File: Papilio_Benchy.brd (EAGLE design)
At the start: 101.6 x 90.2 mm, 123 parts, among them IC1 FT2232H, IC2 93C46, J1 USB MICRO, SW1 EVQQ2, U1 ATMEGA32U4-XUMU, U2 LTC3419EMS, U3 ATMEGA32U4-XUAU, U5 ARDUINO_MEGA_SHIELD, X2 12MHz, Y1 16MHz KX-7

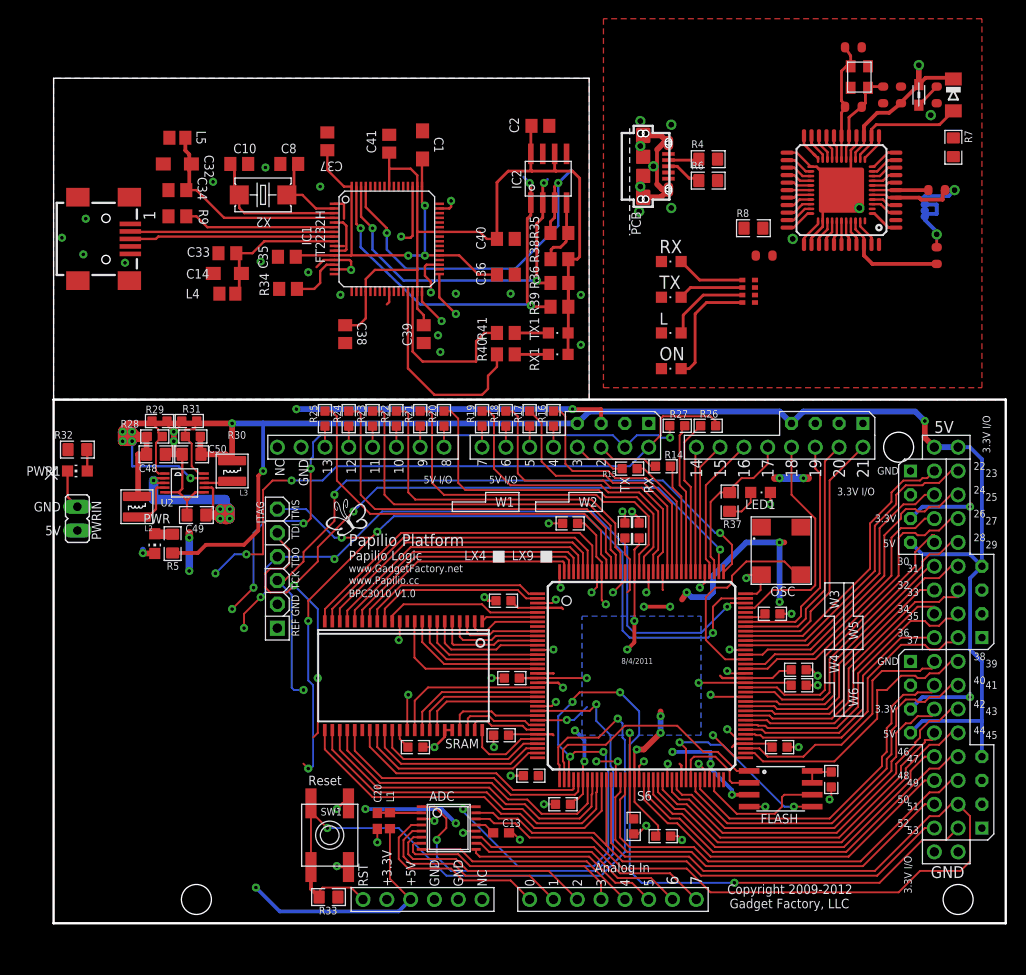
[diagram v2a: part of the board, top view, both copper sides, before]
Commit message: Connections added and blocks placed.
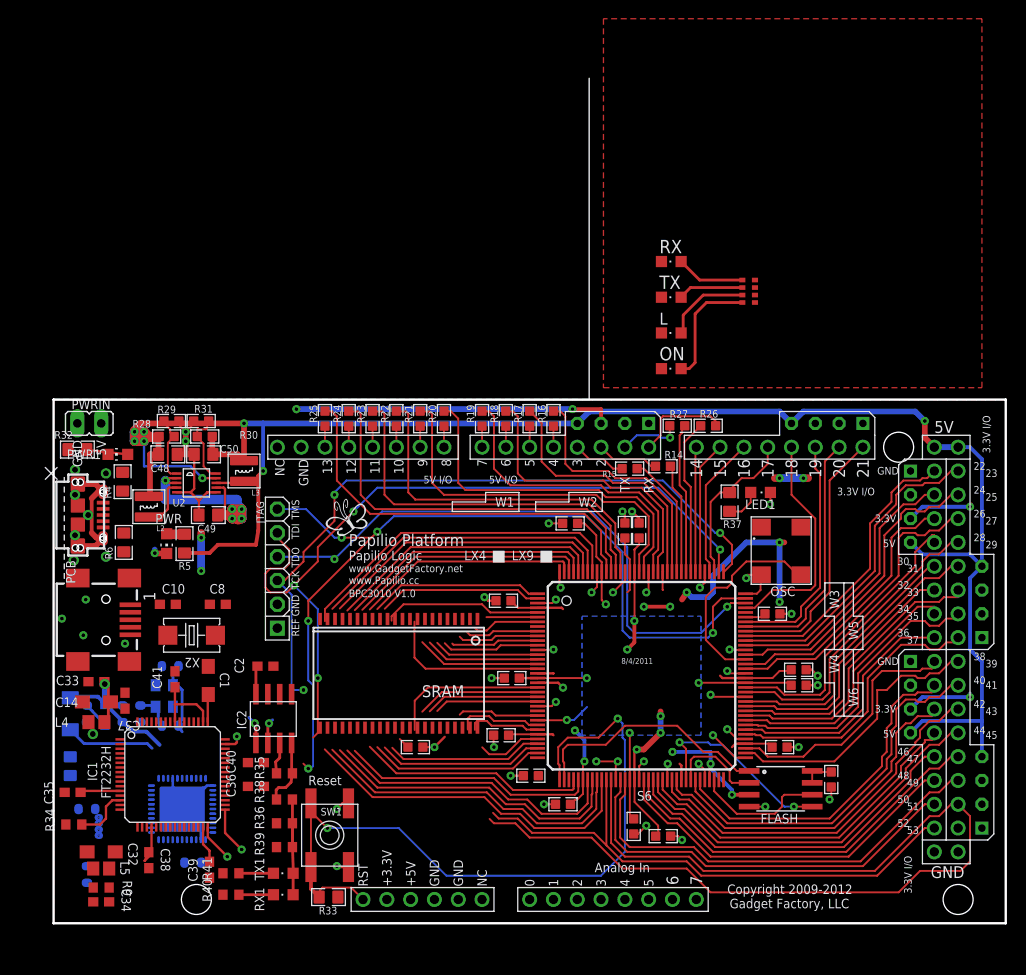
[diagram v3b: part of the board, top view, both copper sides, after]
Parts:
- removed ADC: ADC088S102CIMT, spiadc:TSSOP16
- removed C13, C20: .1uF, rcl:C0603
- removed L1: FERRITEBEAD, rcl:R0603
- removed R8: 10K, GadgetFactory_6.0:0805
- removed U3: ATMEGA32U4-XUAU, SmartPrj:TQFP44-PAD
- C10, C2, C33, C34, C35, C36, C37, C38, C39, C40, C41, C8: device dp_devices:C805 -> dp_devices:C603
- L4, L5: device dp_devices:FB805 -> dp_devices:FB603
- R34, R35, R36, R38, R39, R40, R41, R9: device dp_devices:R805 -> dp_devices:R603
- SRAM: value IS61WV25616 -> ISSI_SRAM_8BIT; device Bogdan_Commons:TSOP44-II -> GadgetFactory:TSOP44-II
- moved D2 115.1 mm to (1.78, 21.1), flipped to the bottom
- moved R7 115.1 mm to (1.78, 15.5), flipped to the bottom
- moved C5 112.2 mm to (3.56, 21.1), flipped to the bottom
- moved C6 112.2 mm to (3.56, 3.94), flipped to the bottom
- moved C7 112.2 mm to (3.56, 10.9), flipped to the bottom
- moved R2 110.1 mm to (4.83, 8.74)
- moved R3 110.1 mm to (4.83, 9.37)
- moved L6 109.1 mm to (5.46, 21.1), flipped to the bottom
- moved C3 106.1 mm to (7.37, 21.1), flipped to the bottom
- moved C9 103.2 mm to (9.27, 21.1), flipped to the bottom
- moved Y1 99.3 mm to (11.8, 23.0), flipped to the bottom
- moved C11 98.4 mm to (12.4, 26.2), flipped to the bottom
- moved R1 98.4 mm to (12.4, 19.8), flipped to the bottom
- moved U1 96.5 mm to (13.7, 10.9), flipped to the bottom
- moved C4 88.9 mm to (14.9, 5.21), flipped to the bottom
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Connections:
- removed net AD0: IC1.16
- removed net AD1: IC1.17
- removed net AD2: IC1.18
- removed net AD3: IC1.19
- removed net ADC_CS: ADC.1, S6.26
- removed net BD0: IC1.38
- removed net BD1: IC1.39
- removed net BD2: IC1.40
- removed net BD3: IC1.41
- removed net D0/RX: U1.20, U3.20
- removed net D1/TX: U1.21, U3.21
- removed net D10: S6.34, SRAM.31
- removed net D11: S6.33, SRAM.32
- removed net D12: S6.21, SRAM.35
- removed net D13: S6.22, SRAM.36
- removed net D14: S6.23, SRAM.37
- removed net D15: S6.24, SRAM.38
- removed net D2/SDA: U1.19, U3.19
- removed net D3/SCL: U1.18, U3.18
- removed net D5*: U1.31, U3.31
- removed net D6*: U1.27, U3.27
- removed net D8: S6.40, SRAM.29
- removed net D9: S6.35, SRAM.30
- removed net HWB: R8.2, U1.33, U3.33
- removed net IO10*: U1.30, U3.30
- removed net IO11*: U1.12, U3.12
- removed net IO12: U1.26, U3.26
- removed net IO13*: RN2.2, U1.32, U3.32
- removed net IO8: U1.28, U3.28
- removed net IO9*: U1.29, U3.29
- removed net MISO: U1.11, U3.11
- removed net MOSI: U1.10, U3.10
- removed net N$10: ADC.2, C20.1, L1.1
- removed net NC: S6.8
- removed net RXLED: RX.C, U1.8, U3.8
- removed net SCK: U1.9, U3.9
- removed net TCK: S6.109, U$2.JTAG_TCK
- removed net TDI: S6.110, U$2.JTAG_TDI
- removed net TDO: S6.106, U$2.JTAG_TDO
- removed net TMS: S6.107, U$2.JTAG_TMS
- removed net TXLED: TX.C, U1.22, U3.22
- new net A18: S6.40, SRAM.41
- new net A19: S6.35, SRAM.25
- new net A20: S6.33, SRAM.42
- new net AD0-JTAG_TCK: IC1.16, S6.109, S6.8, U$2.JTAG_TCK
- new net AD1-JTAG_TDI: IC1.17, S6.110, S6.22, U$2.JTAG_TDI
- new net AD2-JTAG_TDO: IC1.18, S6.106, U$2.JTAG_TDO
- new net AD3-JTAG_TMS: IC1.19, S6.107, U$2.JTAG_TMS
- new net ARDUINO_RESET: D2.A, R7.1, S6.34, U1.13
- new net ATMEGA_A0: U1.36
- new net ATMEGA_A1: U1.37
- new net ATMEGA_A2: U1.38
- new net ATMEGA_A3: U1.39
- new net ATMEGA_A4: U1.40
- new net ATMEGA_A5: U1.41
- new net ATMEGA_D0/RX: U1.20
- new net ATMEGA_D1/TX: U1.21
- new net ATMEGA_D2/SDA: U1.19
- new net ATMEGA_D3/SCL: U1.18
- new net ATMEGA_D4: U1.25
- new net ATMEGA_D5*: U1.31
- new net ATMEGA_D6*: U1.27
- new net ATMEGA_D7: U1.1
- new net ATMEGA_HWB: U1.33
- new net ATMEGA_IO10*: U1.30
- new net ATMEGA_IO11*: U1.12
- new net ATMEGA_IO12: U1.26
- new net ATMEGA_IO13*: RN2.2, U1.32
- new net ATMEGA_IO8: U1.28
- new net ATMEGA_IO9*: U1.29
- new net ATMEGA_MISO: U1.11
- new net ATMEGA_MOSI: U1.10
- new net ATMEGA_RXLED: RX.C, U1.8
- new net ATMEGA_SCK: U1.9
- new net ATMEGA_TXLED: TX.C, U1.22
- new net BD0_MPSSE_TCK: IC1.38, S6.21
- new net BD1_MPSSE_TDI: IC1.39, S6.24
- new net BD2_MPSSE_TDO: IC1.40, S6.23
- new net BD3_MPSSE_TMS: IC1.41, S6.26
- net +5V: no longer U3.14, U3.2, U3.34
- net 3V3: no longer ADC.13, C13.1, SRAM.11, SRAM.33
- net 5V0: no longer L1.2
- net A0: now also SRAM.3; no longer SRAM.1, U1.36, U3.36
- net A1: now also SRAM.4; no longer SRAM.2, U1.37, U3.37
- net A10: now also SRAM.26; no longer SRAM.23
- net A11: now also SRAM.27; no longer SRAM.24
- net A12: now also SRAM.28; no longer SRAM.25
- net A13: now also SRAM.29; no longer SRAM.26
- net A14: now also SRAM.30; no longer SRAM.27
- net A15: now also SRAM.38; no longer SRAM.42
- net A16: now also SRAM.39; no longer SRAM.43
- net A17: now also SRAM.40; no longer SRAM.44
- net A2: now also SRAM.5; no longer SRAM.3, U1.38, U3.38
- net A3: now also SRAM.6; no longer SRAM.4, U1.39, U3.39
- net A4: now also SRAM.7; no longer SRAM.5, U1.40, U3.40
- net A5: now also SRAM.16; no longer SRAM.18, U1.41, U3.41
- net A6: now also SRAM.17; no longer SRAM.19
- net A7: now also SRAM.18; no longer SRAM.20
- net A8: now also SRAM.19; no longer SRAM.21
- net A9: now also SRAM.20; no longer SRAM.22
- net AGND: no longer U3.43
- net AREF: no longer U3.42
- net AVCC: no longer U3.24, U3.44
- net CS: now also SRAM.8; no longer SRAM.6
- net D0: now also SRAM.9; no longer SRAM.7
- net D1: now also SRAM.10; no longer SRAM.8
- net D2: now also SRAM.13; no longer SRAM.9
- net D3: now also SRAM.14; no longer SRAM.10
- net D4: now also SRAM.31; no longer SRAM.13, U1.25, U3.25
- net D5: now also SRAM.32; no longer SRAM.14
- net D6: now also SRAM.35; no longer SRAM.15
- net D7: now also SRAM.36; no longer SRAM.16, U1.1, U3.1
- net GND: no longer ADC.12, ADC.3, C13.2, C20.2, R8.1, SRAM.39, SRAM.40, U3.15, U3.23, U3.35, U3.P$1
- net MEGA_A0: no longer ADC.4
- net MEGA_A1: no longer ADC.5
- net MEGA_A2: no longer ADC.6
- net MEGA_A3: no longer ADC.7
- net MEGA_A4: no longer ADC.8
- net MEGA_A5: no longer ADC.9
- net MEGA_A6: no longer ADC.10
- net MEGA_A7: no longer ADC.11
- net MEGA_D51: no longer ADC.14
- net MEGA_D52: no longer ADC.15
- net MEGA_D53: no longer ADC.16
- net OE: now also SRAM.37; no longer SRAM.41
- net RD+: no longer U3.4
- net RD-: no longer U3.3
- net RESET: no longer D2.A, R7.1, U1.13, U3.13
- net UCAP: no longer U3.6
- net UGND: no longer U3.5
- net VUSB: no longer U3.7
- net WE: now also SRAM.15; no longer SRAM.17
- net XTAL1: no longer U3.17
- net XTAL2: no longer U3.16
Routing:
- net MEGA_D53: track 108.4 -> 0.00 mm, vias 6 -> 0
- net AD1-JTAG_TDI: track 0.00 -> 98.7 mm, vias 0 -> 4
- net TMS: track 94.5 -> 0.00 mm, vias 5 -> 0
- net AD3-JTAG_TMS: track 0.00 -> 94.5 mm, vias 0 -> 5
- net TDI: track 85.5 -> 0.00 mm, vias 4 -> 0
- net TCK: track 74.9 -> 0.00 mm, vias 3 -> 0
- net AD0-JTAG_TCK: track 0.00 -> 74.9 mm, vias 0 -> 3
- net TDO: track 73.2 -> 0.00 mm, vias 4 -> 0
- net AD2-JTAG_TDO: track 0.00 -> 64.1 mm, vias 0 -> 2
- net GND: track 188.1 -> 124.5 mm, vias 78 -> 55
- net USB_RXD: track 65.1 -> 6.74 mm, vias 5 -> 1
- net 3.3V: track 89.5 -> 32.9 mm
- net USB_TXD: track 66.1 -> 10.3 mm, vias 3 -> 0
- net ADC_CS: track 51.1 -> 0.00 mm, vias 2 -> 0
- net EECS: track 43.8 -> 3.04 mm, vias 3 -> 1
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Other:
- outline, holes or cut-outs redrawn
- board text removed: "!PWEREN"
- board text removed: "!RESET"
- board text removed: "1.8V"
- board text removed: "3V3"
- board text removed: "ACBUS0"
- board text removed: "ACBUS1"
- board text removed: "ACBUS2"
- board text removed: "ACBUS3"
- board text removed: "ACBUS4"
- board text removed: "ACBUS5"
- board text removed: "ACBUS6"
- board text removed: "ACBUS7"
- board text removed: "ADBUS0"
- board text removed: "ADBUS1"
- board text removed: "ADBUS2"
- board text removed: "ADBUS3"
- board text removed: "ADBUS4"
- board text removed: "ADBUS5"
- board text removed: "ADBUS6"
- board text removed: "ADBUS7"
- board text removed: "BCBUS0"
- board text removed: "BCBUS1"
- board text removed: "BCBUS2"
- board text removed: "BCBUS3"
- board text removed: "BCBUS4"
- board text removed: "BCBUS5"
- board text removed: "BCBUS6"
- board text removed: "BCBUS7"
- board text removed: "BDBUS0"
- board text removed: "BDBUS1"
- board text removed: "BDBUS2"
- board text removed: "BDBUS3"
- board text removed: "BDBUS4"
- board text removed: "BDBUS5"
- board text removed: "BDBUS6"
- board text removed: "BDBUS7"
- board text removed: "Dangerous Prototypes"
- board text removed: "EECLK"
- board text removed: "EECS"
- board text removed: "EEDATA"
- board text removed: "FT2232H Breakout Board v1a"
- board text removed: "Fulfillment By:"
- board text removed: "ITALY"
- board text removed: "MADE IN"
- board text removed: "Seeed Studio"
- board text removed: "X2"
- board text removed: "dangerousprototypes.com"
- board text removed: "seeedstudio.com"

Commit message: Bunch of little changes
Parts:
- added R8: 4.7K, GadgetFactory:0603
- moved PWRIN 2.84 mm to (6.35, 53.3)
- moved TX 1.27 mm to (65.9, 66.8)
- moved C10 1.27 mm to (12.2, 34.0)
- moved C17 1.27 mm to (76.7, 33.0)
- moved C28 1.27 mm to (48.0, 34.4)
- moved C49 1.27 mm to (16.5, 43.6)
- moved C8 1.27 mm to (17.5, 34.0)
- moved J1 1.27 mm to (2.59, 43.6)
- moved L2 1.27 mm to (10.2, 44.5)
- moved ON 1.27 mm to (65.9, 59.2)
- moved R14 1.27 mm to (65.0, 48.8)
- moved R15 1.27 mm to (61.5, 48.5)
- moved R29 1.27 mm to (12.6, 53.6)
- moved R31 1.27 mm to (15.7, 53.6)
- moved R6 1.27 mm to (7.49, 40.6)
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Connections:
- removed net ATMEGA_HWB: U1.33
- removed net ATMEGA_MISO: U1.11
- removed net ATMEGA_MOSI: U1.10
- removed net ATMEGA_SCK: U1.9
- removed net MEGA_A0: U5.A0
- removed net MEGA_A1: U5.A1
- removed net MEGA_A2: U5.A2
- removed net MEGA_A3: U5.A3
- removed net MEGA_A4: U5.A4
- removed net MEGA_A5: U5.A5
- removed net MEGA_A6: U5.A6
- removed net MEGA_A7: U5.A7
- removed net N$11: R15.2, U5.D3
- removed net N$12: R16.2, U5.D4
- removed net N$13: R17.2, U5.D5
- removed net N$14: R18.2, U5.D6
- removed net N$15: R19.2, U5.D7
- removed net N$16: R20.2, U5.D8
- removed net N$17: R21.2, U5.D9
- removed net N$18: R22.2, U5.D10
- removed net N$19: R23.2, U5.D11
- removed net N$20: R24.2, U5.D12
- removed net N$21: R25.2, U5.D13
- removed net N$6: R14.2, U5.D2
- removed net USB_RXD: R26.2, U5.TX
- removed net USB_TXD: R27.2, U5.RX
- new net NC1: S6.22
- new net NC2: S6.8
- net 3V3: now also R8.2
- net 5V0: no longer U5.5V@1, U5.5V@2
- net AD0-JTAG_TCK: no longer S6.8
- net AD1-JTAG_TDI: no longer S6.22
- net ATMEGA_A0: now also U5.A0
- net ATMEGA_A1: now also U5.A1
- net ATMEGA_A2: now also U5.A2
- net ATMEGA_A3: now also U5.A3
- net ATMEGA_A4: now also U5.A4
- net ATMEGA_A5: now also U5.A5
- net ATMEGA_D0/RX: now also R27.2, U5.RX
- net ATMEGA_D1/TX: now also R26.2, U5.TX
- net ATMEGA_D2/SDA: now also R14.2, U5.D2
- net ATMEGA_D3/SCL: now also R15.2, U5.D3
- net ATMEGA_D4: now also R16.2, U5.D4
- net ATMEGA_D5*: now also R17.2, U5.D5
- net ATMEGA_D6*: now also R18.2, U5.D6
- net ATMEGA_D7: now also R19.2, U5.D7
- net ATMEGA_IO10*: now also R22.2, U5.D10
- net ATMEGA_IO11*: now also R23.2, U5.D11
- net ATMEGA_IO12: now also R24.2, U5.D12
- net ATMEGA_IO13*: now also R25.2, U5.D13
- net ATMEGA_IO8: now also R20.2, U5.D8
- net ATMEGA_IO9*: now also R21.2, U5.D9
- net GND: now also U1.33
- net MEGA_D51: now also U1.9
- net MEGA_D52: now also U1.10
- net MEGA_D53: now also R8.1, U1.11
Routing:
- net NC1: track 0.00 -> 13.2 mm
- net AD1-JTAG_TDI: track 98.7 -> 85.5 mm
- net USB_TXD: track 10.3 -> 0.00 mm
- net ATMEGA_D0/RX: track 0.00 -> 10.3 mm
- net 5V0: track 170.7 -> 161.9 mm
- net USB_RXD: track 6.74 -> 0.00 mm, vias 1 -> 0
- net ATMEGA_D1/TX: track 0.00 -> 6.74 mm, vias 0 -> 1
- net N$6: track 6.65 -> 0.00 mm
- net ATMEGA_D2/SDA: track 0.00 -> 6.65 mm
- net N$11: track 5.73 -> 0.00 mm
- net ATMEGA_D3/SCL: track 0.00 -> 5.73 mm
- net ATMEGA_IO9*: track 0.00 -> 2.25 mm
- net ATMEGA_IO8: track 0.00 -> 2.25 mm
- net ATMEGA_IO13*: track 0.00 -> 2.25 mm
- net ATMEGA_IO12: track 0.00 -> 2.25 mm
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
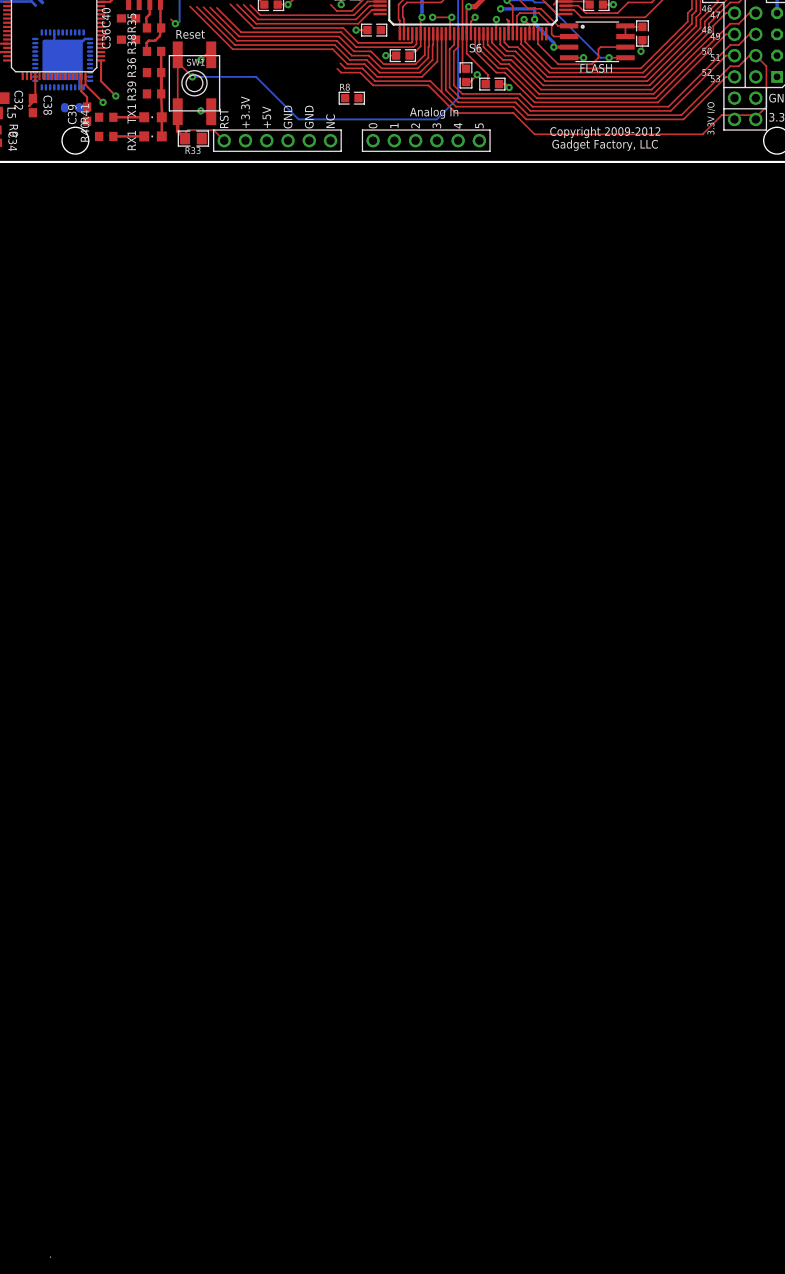
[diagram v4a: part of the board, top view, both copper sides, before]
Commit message: Added switch and HDMI
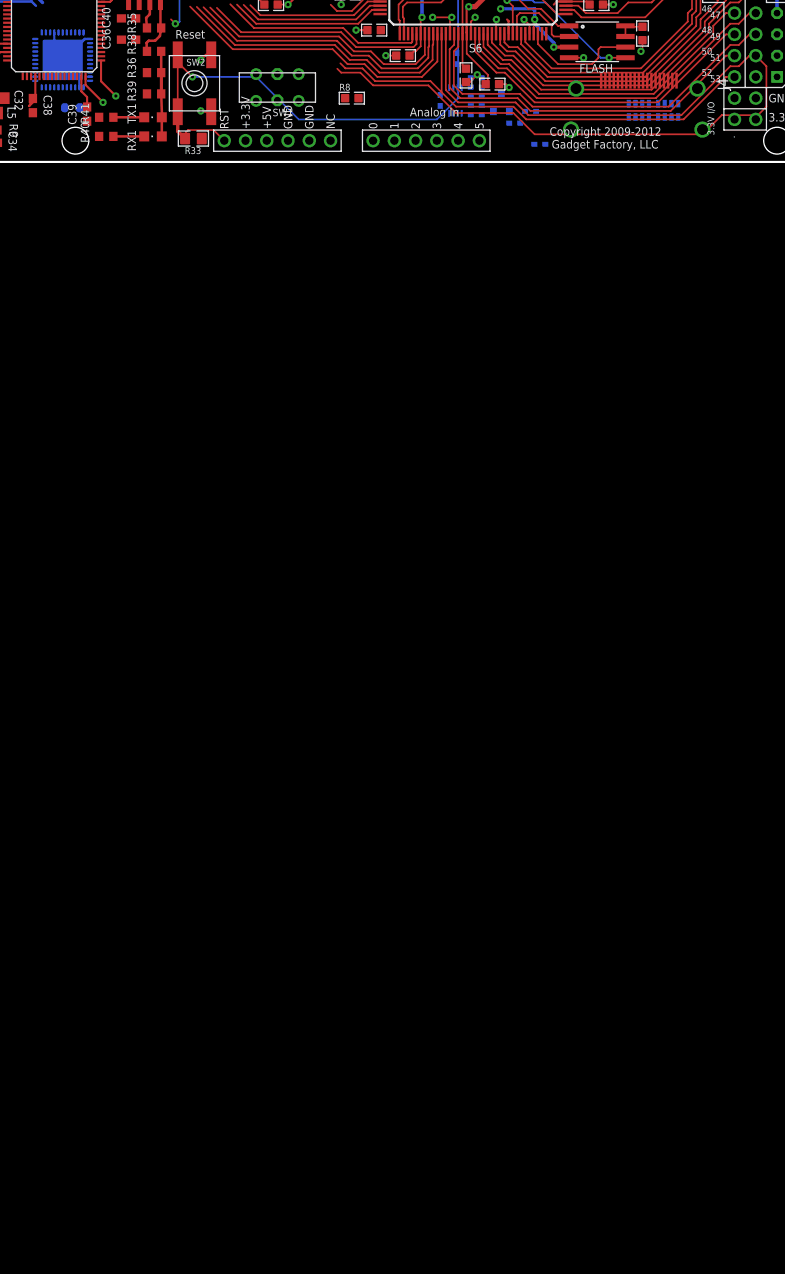
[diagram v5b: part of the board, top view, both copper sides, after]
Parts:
- added C20: 1uF, saanlima:0402
- added J4: HDMI-TYPE-A-RECEPTICALFCI10029449, saanlima:FCI-HDMI-TYPE-A-RECEPT
- added R10, R45: 10K, saanlima:0402
- added R11: 0, saanlima:0402
- added R12, R13, R42, R43: 1K, saanlima:0402
- added R44: 100K, saanlima:0402
- added R46: 2.2K, saanlima:0402
- added RN1, RN3: 51, saanlima:CTS742C083
- added SW2: EVQQ2, adafruit:EVQ-Q2
- added T1: MOSFET-NCHANNELSMD, saanlima:SOT23-3
- added U11: PCA9306, saanlima:PSOP-8
- SW1: value EVQQ2 -> SWITCH-2CH-6P-3010010P1; device adafruit:EVQ-Q2 -> OPL Eagle Library:6P-2CH-2.54-9.1X3.5X3.2+2H
- moved SW1 9.92 mm to (39.4, 8.89), turned to 180 degrees
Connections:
- new net DDC_SCL: J4.15, R42.2, U11.6
- new net DDC_SDA: J4.16, R43.2, U11.5
- new net DETECT: J4.19, R10.2, R45.1
- new net FPGA_SCL: R12.2, U11.3
- new net FPGA_SDA: R13.2, U11.4
- new net HDMI_DET#: R46.2, T1.3
- new net N$17: R45.2, T1.1
- new net N$6: C20.1, R44.1, U11.7, U11.8
- new net SW0: S6.104, SW1.COM2
- new net TX_HDMI_5V: J4.18, R11.1, R42.1, R43.1, R44.2
- net 3V3: now also R12.1, R13.1, R46.1, RN1.5, RN1.6, RN1.7, RN1.8, RN3.5, RN3.6, RN3.7, RN3.8, SW1.CH2A, U11.2
- net 5V: now also R11.2
- net GND: now also C20.2, J4.11, J4.14, J4.17, J4.2, J4.5, J4.8, R10.1, SW1.CH2B, SW2.B, SW2.B', T1.2, U11.1; no longer SW1.B, SW1.B'
- net MEGA_D45: now also J4.1, RN1.4
- net MEGA_D46: now also J4.3, RN1.3
- net MEGA_D47: now also J4.4, RN1.2
- net MEGA_D48: now also J4.6, RN1.1
- net MEGA_D49: now also J4.10, RN3.2
- net MEGA_D50: now also J4.12, RN3.1
- net MEGA_D51: now also J4.7, RN3.4
- net MEGA_D52: now also J4.9, RN3.3
- net MEGA_D53: now also J4.13
- net RESET: now also SW2.A, SW2.A'; no longer SW1.A, SW1.A'
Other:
- board text added: "C20"
- board text added: "J4"
- board text added: "R14"
- board text added: "R17"
- board text added: "R18"
- board text added: "R19"
- board text added: "R22"
- board text added: "R25"
- board text added: "R26"
- board text added: "RN1"
- board text added: "RN2"
- board text added: "T1"
- board text added: "U11"
